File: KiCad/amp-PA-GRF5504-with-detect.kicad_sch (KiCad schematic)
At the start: 51 parts, among them J1 142-0701-851, J2 142-0701-851, Q1 P-CH, Q2 N-CH, U2 BDCN-20-13+, U3 LT5534, U4 LT5534, U5 GRF5504

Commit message: cleared all ERC warnings
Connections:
- net GND: no longer J1.GND3 (GND), J2.GND3 (GND)
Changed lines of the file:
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@@
 			)
 		)
-		(pin "GND3"
-		)
 		(pin "GND4"
 		)
@@
 	)
 	(symbol
+		(lib_name "142-0701-851_1")
 		(lib_id "amp-PA-TQP7M9105-with-detect-eagle-import:142-0701-851")
 		(at 36.83 205.74 0)
@@
 		(pin "GND4"
 		)
-		(pin "GND3"
-		)
 		(pin "RF1"

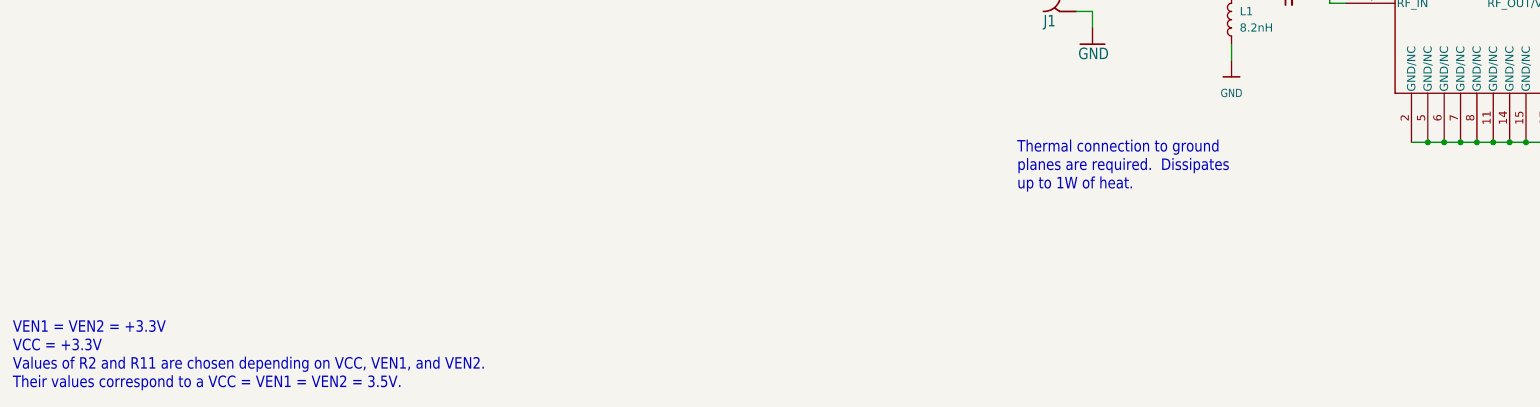
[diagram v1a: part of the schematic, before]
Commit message: updated comments on schematic
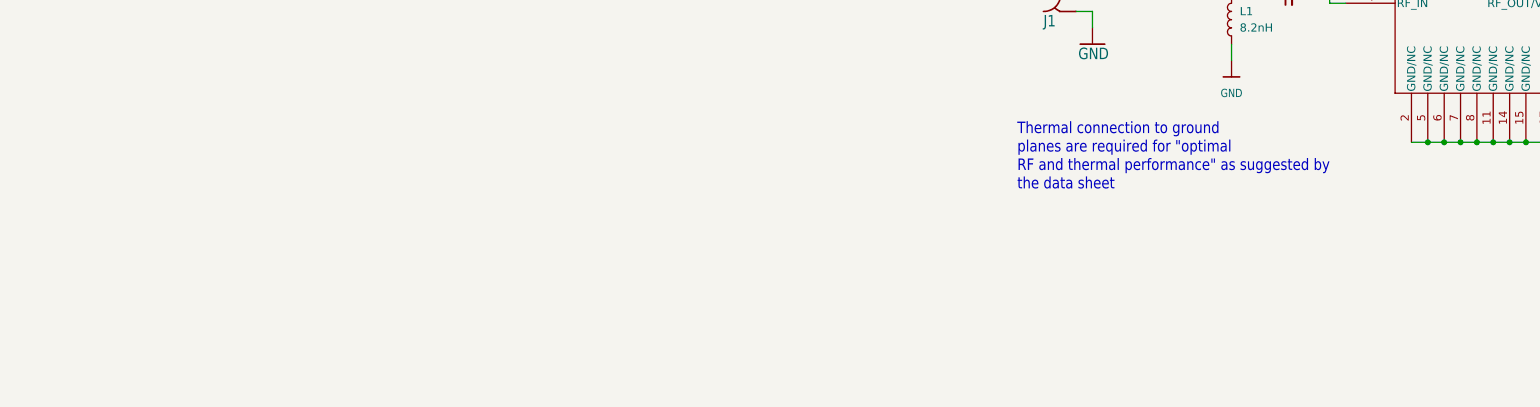
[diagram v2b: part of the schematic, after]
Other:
- note added: "Thermal connection to ground planes are required for "optimal RF and thermal performance" as suggested by the data sheet"
- note removed: "Thermal connection to ground planes are required. Dissipates up to 1W of heat."
- note removed: "VEN1 = VEN2 = +3.3V VCC = +3.3V Values of R2 and R11 are chosen depending on VCC, VEN1, and VEN2. Their values correspond to a VCC = VEN1 = VEN2 = 3.5V."
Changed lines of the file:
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@@
-		)
-	)
-	(text "VEN1 = VEN2 = +3.3V\nVCC = +3.3V\nValues of R2 and R11 are chosen depending on VCC, VEN1, and VEN2.\nTheir values correspond to a VCC = VEN1 = VEN2 = 3.5V.\n\n\n"
-		(exclude_from_sim no)
-		(at -125.73 272.796 0)
-		(effects
-			(font
-				(size 1.778 1.5113)
-			)
-			(justify left bottom)
 		)
 	)
@@
 		)
 	)
-	(text "Thermal connection to ground\nplanes are required.  Dissipates\nup to 1W of heat."
+	(text "Thermal connection to ground\nplanes are required for \"optimal\nRF and thermal performance\" as suggested by\nthe data sheet\n"
 		(exclude_from_sim no)
 		(at 30.226 236.22 0)
